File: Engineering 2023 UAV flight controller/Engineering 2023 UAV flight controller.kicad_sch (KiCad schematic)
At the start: 86 parts, among them J1 Micro_SD_Card, J2 ESC speed control, J3 USB_C_Receptacle_USB2.0, J4 Conn_Coaxial, J5 external power rail, J6 Board GPIO and the Lora DIO, J7 external ground rail, M1 Aileron Left, M2 Aileron Right, M3 Elevator Left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

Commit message: pcb revision one completed, the png's are for the reddit gods to review.
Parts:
- removed J6: Board GPIO and the Lora DIO, Connector_PinHeader_2.54mm:PinHeader_1x13_P2.54mm_Vertical, symbol Connector_Generic:Conn_01x13
- added H1, H2, H3: MountingHole, MountingHole:MountingHole_3.2mm_M3, symbol Mechanical:MountingHole
- added J10: DIO, Connector_PinHeader_2.54mm:PinHeader_1x03_P2.54mm_Vertical, symbol Connector_Generic:Conn_01x03
- added J6: GPIO, Connector_PinHeader_2.54mm:PinHeader_1x10_P2.54mm_Vertical, symbol Connector_Generic:Conn_01x10
- added J8: Serial wire debug, Connector_PinHeader_2.54mm:PinHeader_1x02_P2.54mm_Vertical, symbol Connector_Generic:Conn_01x02
- added J9: reset short?, Connector_PinHeader_2.54mm:PinHeader_1x02_P2.54mm_Vertical, symbol Connector_Generic:Conn_01x02
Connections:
- net DIO1: now also J10.1 (Pin_1)
- net DIO2: now also J10.2 (Pin_2)
- net DIO3: now also J10.3 (Pin_3)
- net External_pin_1: now also J6.1 (Pin_1)
- net External_pin_10: now also J6.10 (Pin_10)
- net External_pin_2: now also J6.2 (Pin_2)
- net External_pin_3: now also J6.3 (Pin_3)
- net External_pin_4: now also J6.4 (Pin_4)
- net External_pin_5: now also J6.5 (Pin_5)
- net External_pin_6: now also J6.6 (Pin_6)
- net External_pin_7: now also J6.7 (Pin_7)
- net External_pin_8: now also J6.8 (Pin_8)
- net External_pin_9: now also J6.9 (Pin_9)
- net GND: now also J9.2 (Pin_2)
- net RUN: now also J9.1 (Pin_1)
- net SWCLK: now also J8.1 (Pin_1)
- net SWD: now also J8.2 (Pin_2)
- net IMU_decouple_cap renamed IMU_CPOUT
- net IMU_CPOUT: no longer C25.2, U6.10 (REGOUT)
- new net IMU_REGOUT: C25.2, U6.10 (REGOUT)
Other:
- note removed: "0.1u for pin 10 2n2 for pin 20"

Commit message: got some work to do
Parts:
- removed C2, C6: 0.1uf, Capacitor_SMD:C_0603_1608Metric, symbol Device:C
- removed C5: 1uf, Capacitor_SMD:C_0603_1608Metric, symbol Device:C
- removed H1, H2, H3: MountingHole, MountingHole:MountingHole_3.2mm_M3, symbol Mechanical:MountingHole
- removed R1: R, Resistor_SMD:R_0603_1608Metric, symbol Device:R
- removed R2: R_Trim, Potentiometer_SMD:Potentiometer_Bourns_3314R-GM5_Vertical, symbol Device:R_Trim
- removed U3: LM350_TO220, Package_TO_SOT_THT:TO-220-3_Vertical, symbol Regulator_Linear:LM350_TO220
- added C?: 47u, symbol Device:C_Polarized_Small
- added J?: RFShield_OnePiece, symbol Device:RFShield_OnePiece
- C35: value 47p -> 10n
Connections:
- net GND: now also C?.2, J?.1 (Shield)
- net Servo 6V rail: now also C?.1; no longer D3.2 (A)
- net led_red: no longer names the net of D3.1 (K), R11.1
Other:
- note added: "switching regulator instead of linier reg"
- note removed: "R2/R1 = 4.8"

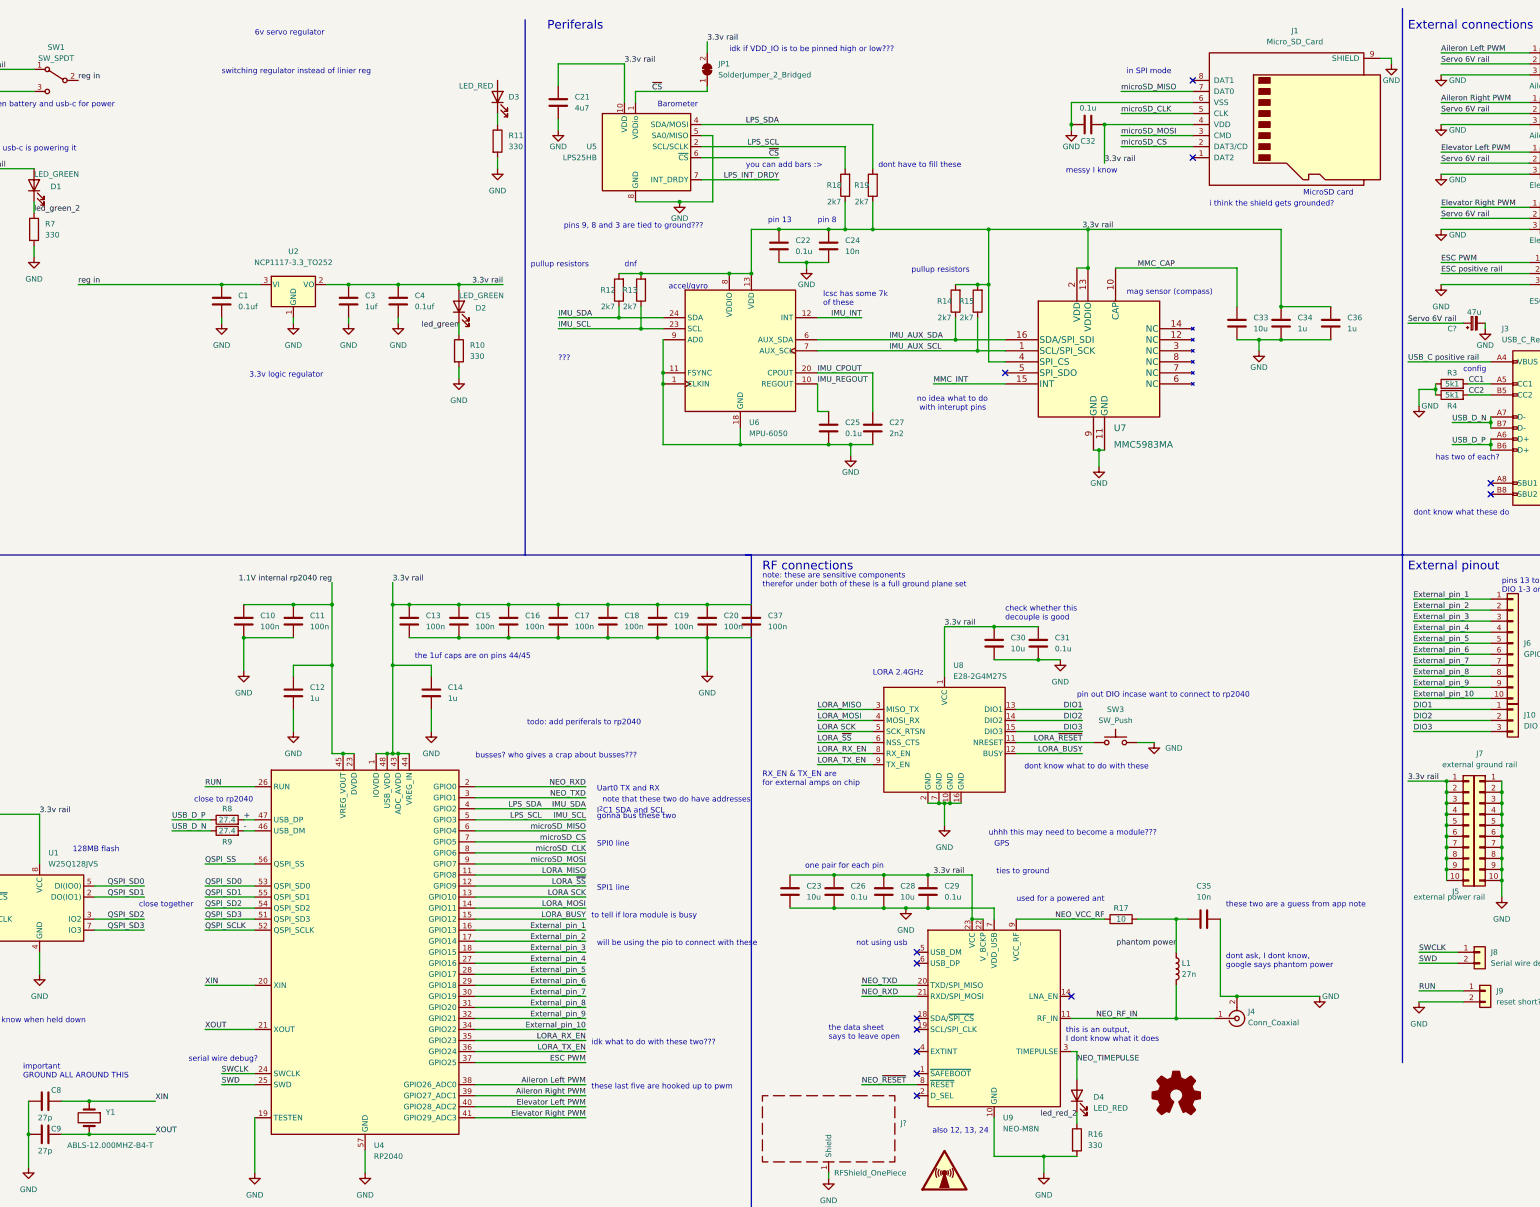
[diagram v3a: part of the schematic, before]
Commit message: added boost regulator
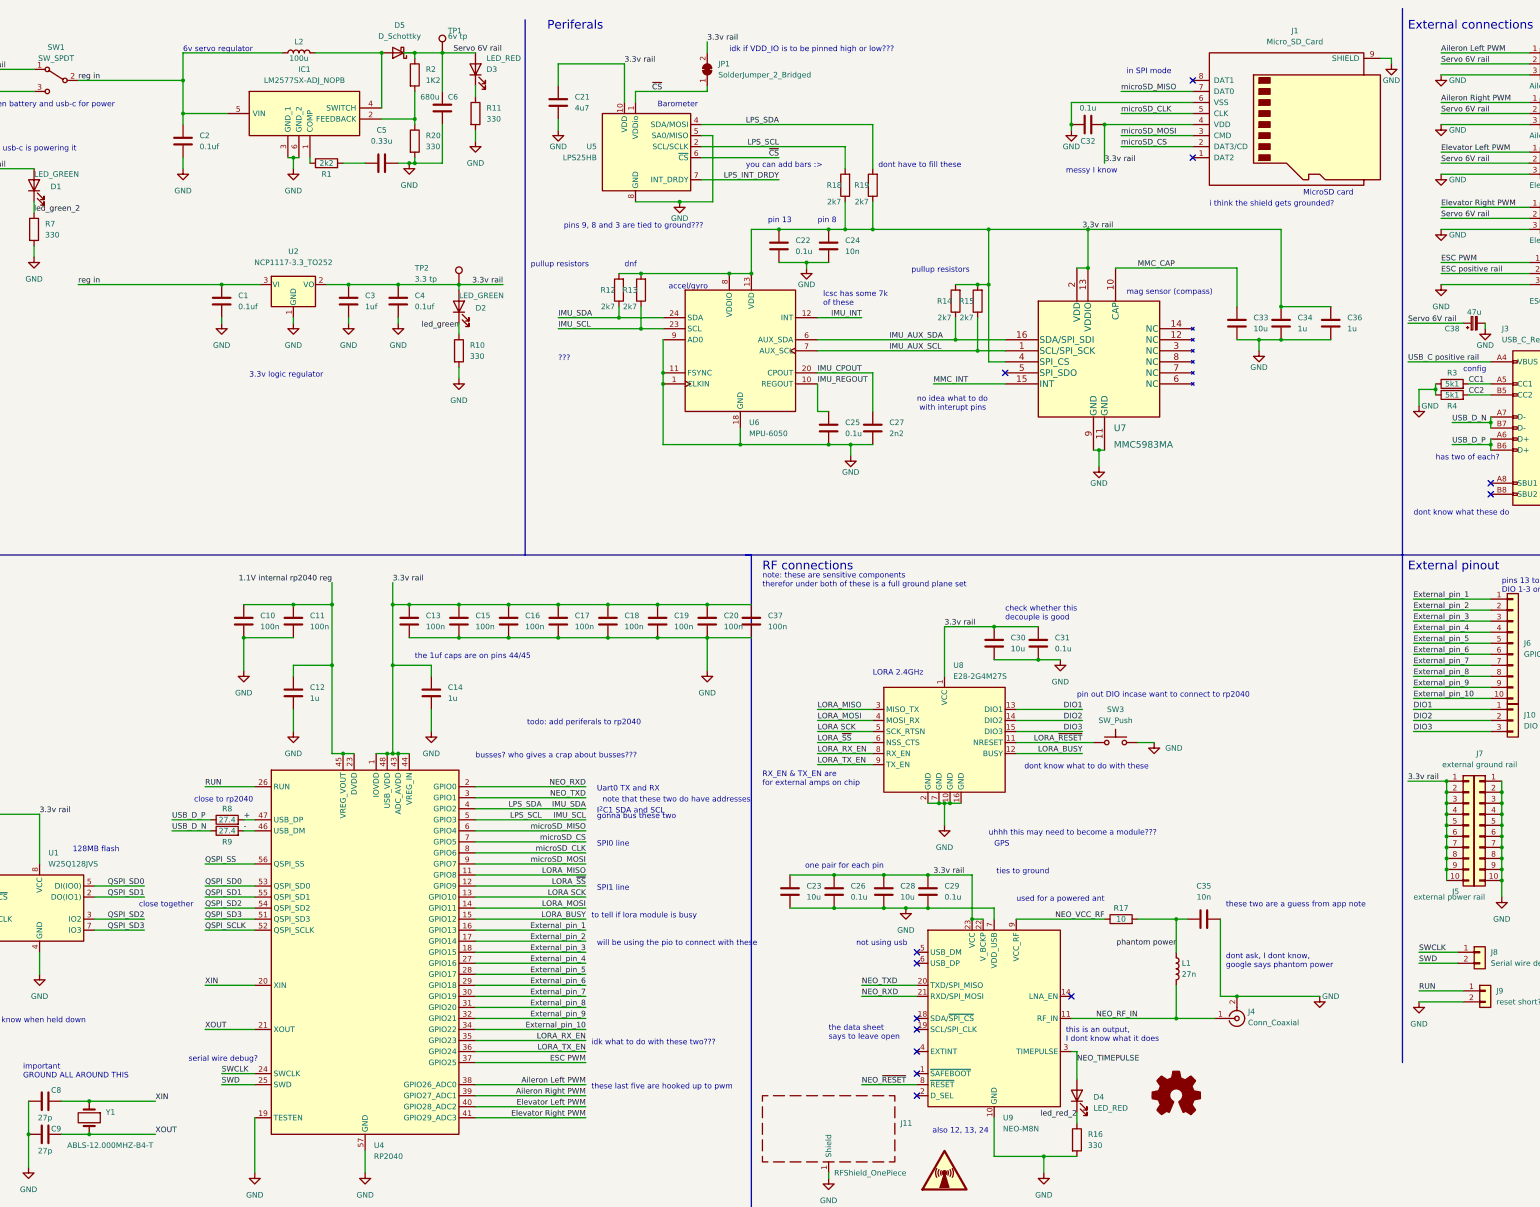
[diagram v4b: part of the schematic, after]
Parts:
- added C2: 0.1uf, Capacitor_SMD:C_0603_1608Metric, symbol Device:C
- added C5: 0.33u, Capacitor_SMD:C_0603_1608Metric, symbol Device:C
- added C6: 680u, Capacitor_SMD:C_0603_1608Metric, symbol Device:C
- added D5: D_Schottky, Diode_SMD:D_SMA, symbol Device:D_Schottky
- added IC1: LM2577SX-ADJ_NOPB, KTT0005B, symbol LM2577SX-ADJ_NOPB:LM2577SX-ADJ_NOPB
- added L2: 100u, symbol Device:L
- added R1: 2k2, Resistor_SMD:R_0603_1608Metric, symbol Device:R
- added R2: 1K2, Resistor_SMD:R_0603_1608Metric, symbol Device:R
- added R20: 330, Resistor_SMD:R_0603_1608Metric, symbol Device:R
- added TP1: 6v tp, TestPoint:TestPoint_Pad_D2.5mm, symbol Connector:TestPoint
- added TP2: 3.3 tp, TestPoint:TestPoint_Pad_D2.5mm, symbol Connector:TestPoint
- gave numbers to parts that had none: 2
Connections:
- net 3.3v rail: now also TP2.1
- net GND: now also C2.2, C5.2, C6.1, IC1.3 (GND_1), IC1.6 (GND_2), R20.2
- net Servo 6V rail: now also D3.2 (A), C6.2, D5.1 (K), R2.1, TP1.1
- net reg in: now also C2.1, IC1.5 (VIN), L2.1
- new net: IC1.2 (FEEDBACK), R2.2, R20.1
- new net: IC1.1 (COMP), R1.1
- new net: D5.2 (A), IC1.4 (SWITCH), L2.2
- new net: C5.1, R1.2
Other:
- note removed: "switching regulator instead of linier reg"
- moved on the sheet: D3, R11

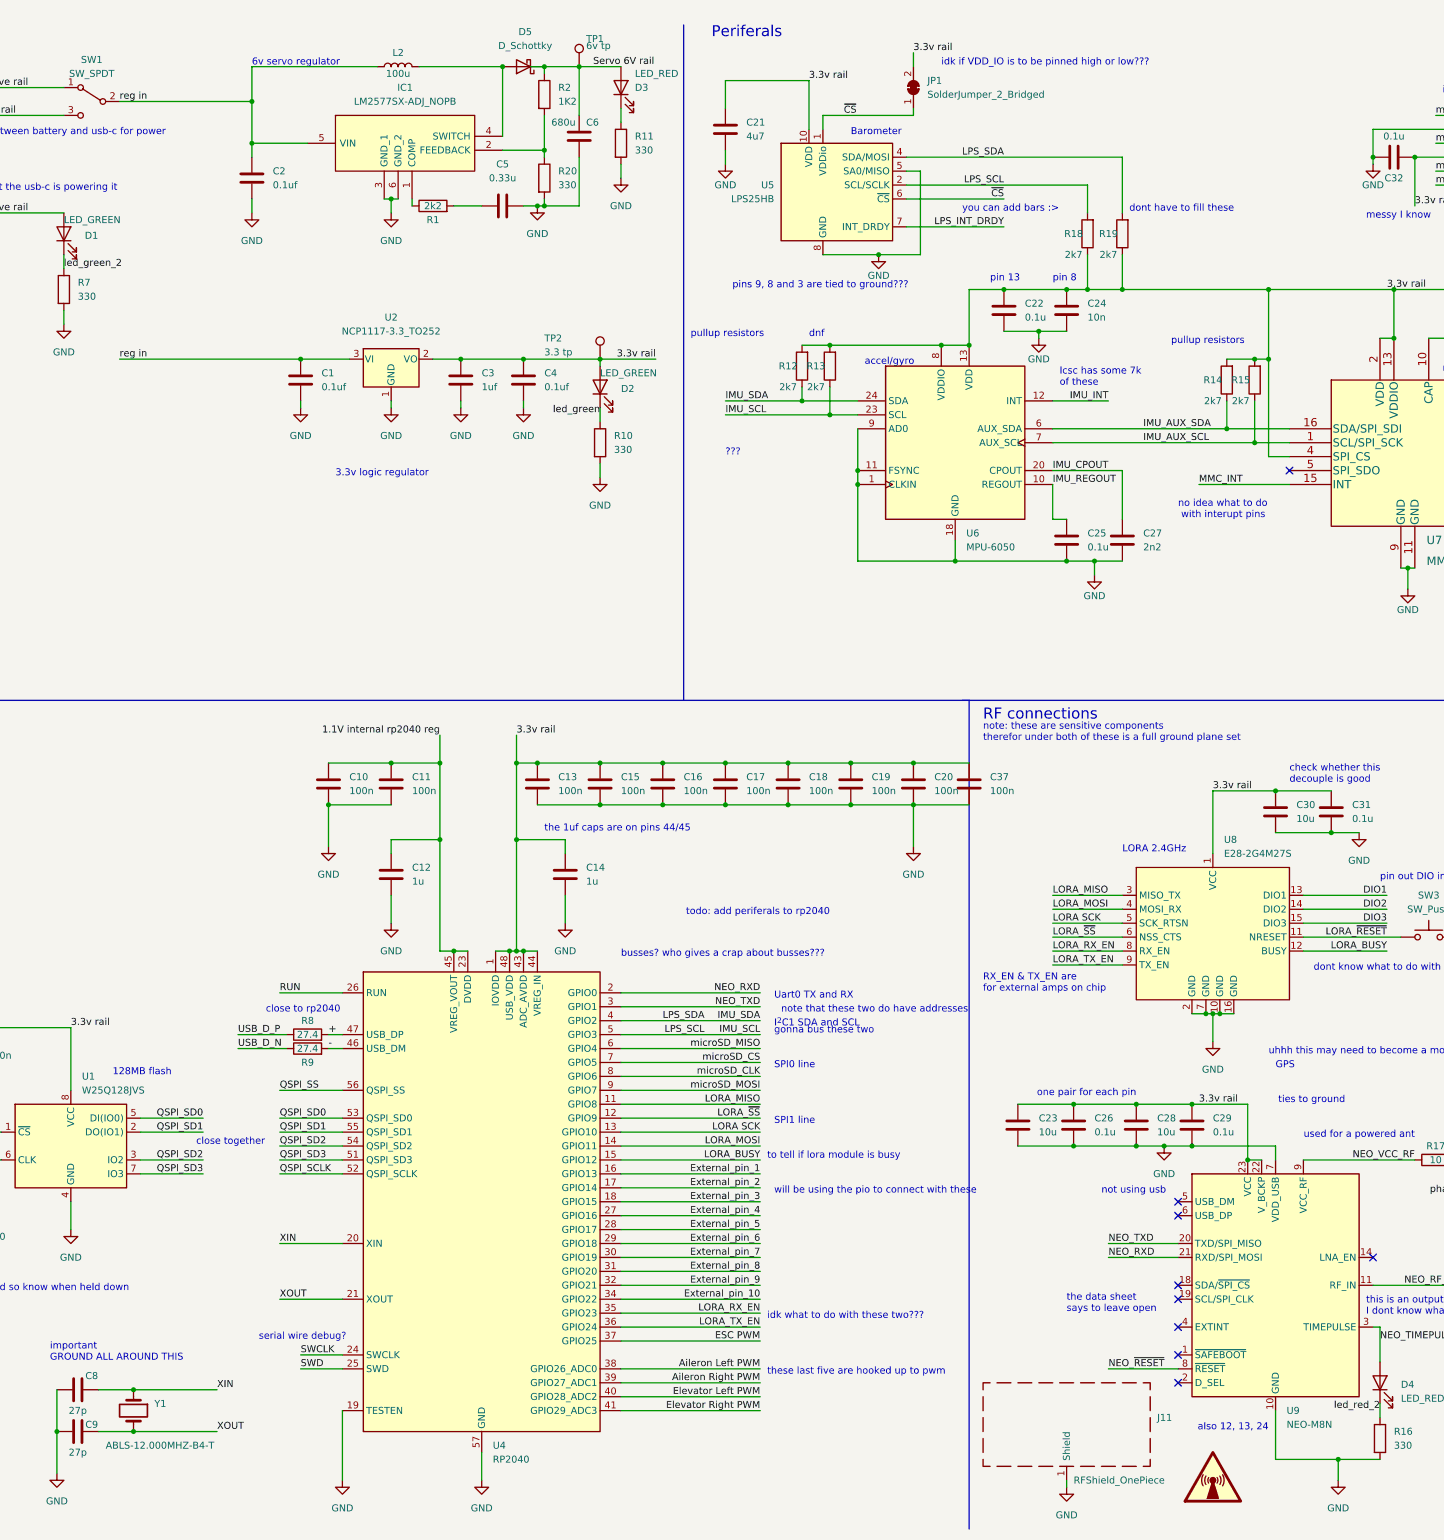
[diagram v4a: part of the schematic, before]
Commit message: started layout for the power part of board, addded some beads to NEO RX/TX
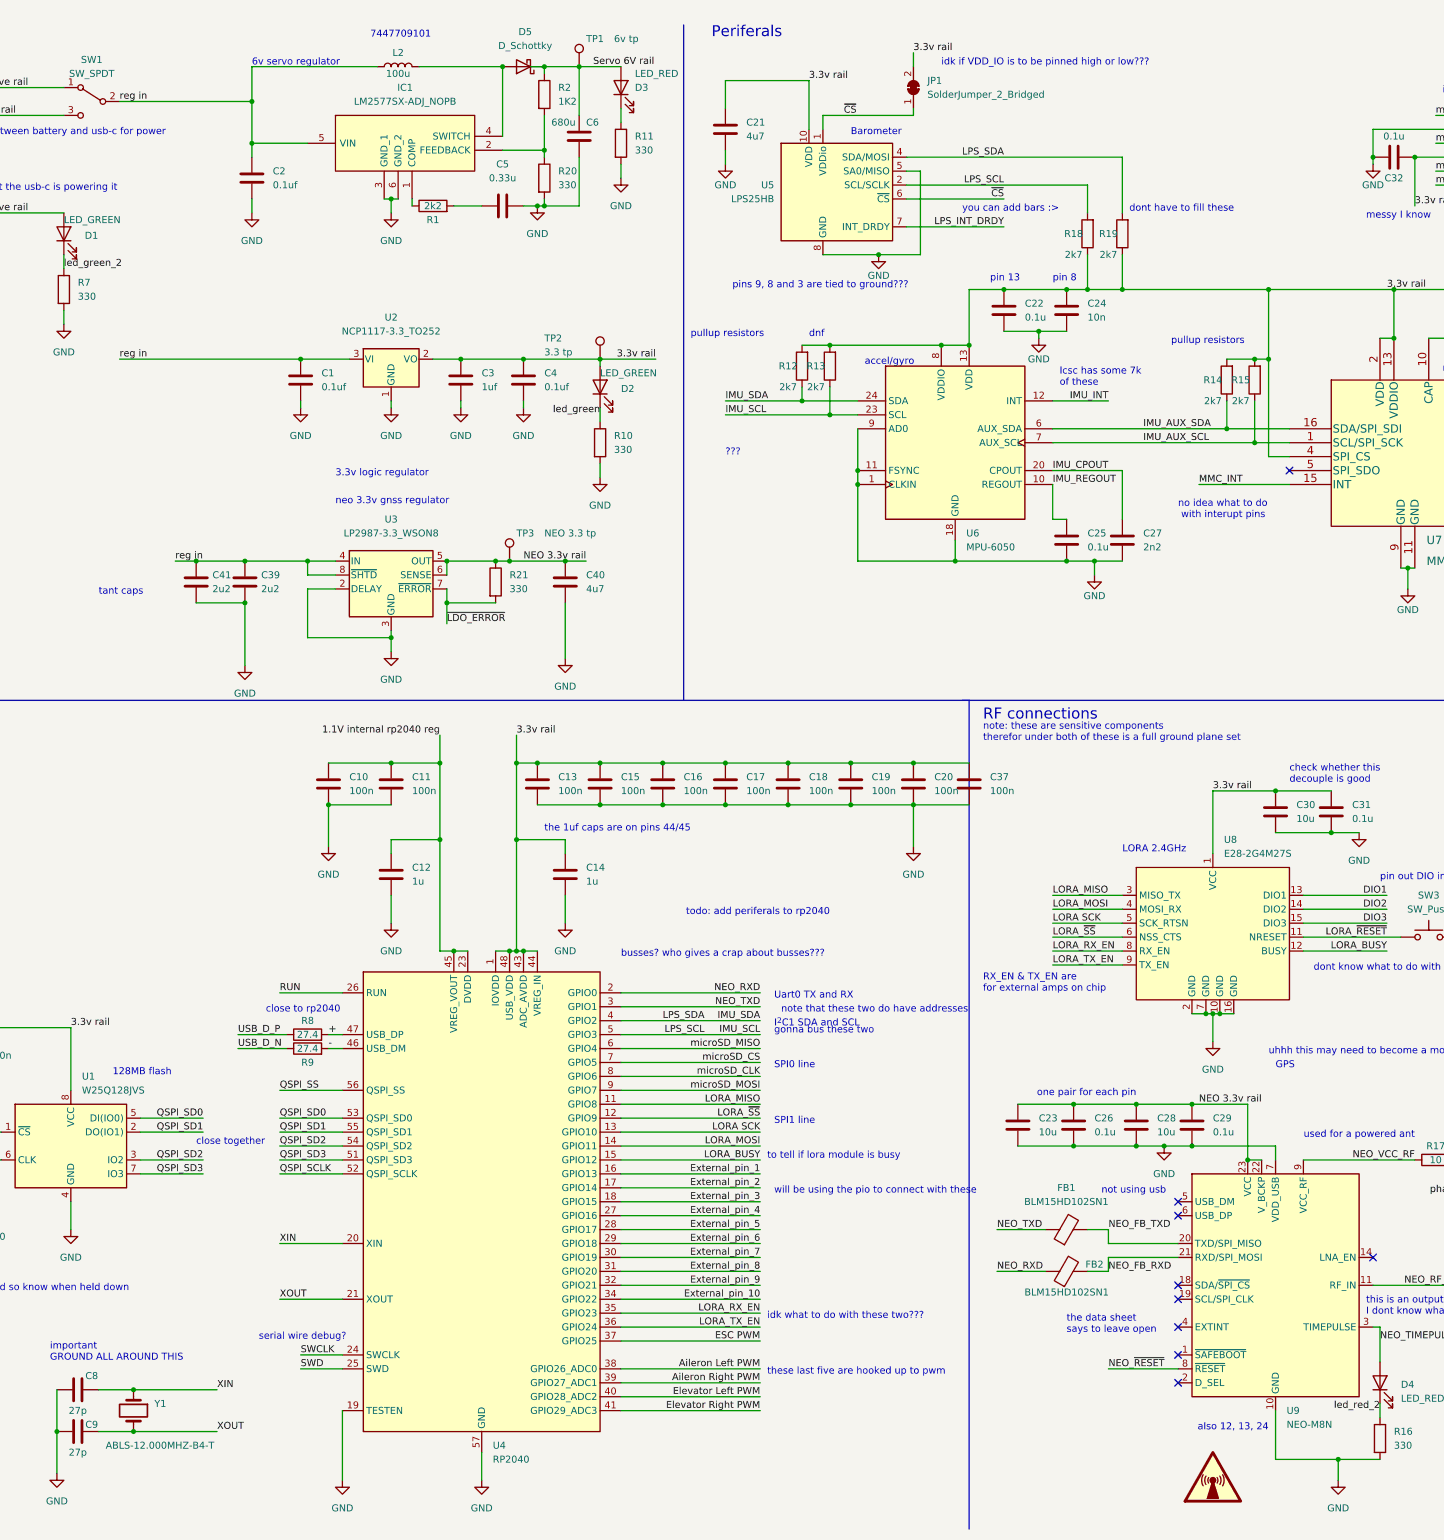
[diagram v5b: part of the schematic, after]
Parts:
- removed J11: RFShield_OnePiece, symbol Device:RFShield_OnePiece
- added C39, C41: 2u2, Capacitor_SMD:C_0603_1608Metric, symbol Device:C
- added C40: 4u7, Capacitor_SMD:C_0603_1608Metric, symbol Device:C
- added FB1, FB2: BLM15HD102SN1, Inductor_SMD:L_0402_1005Metric_Pad0.77x0.64mm_HandSolder, symbol Device:FerriteBead
- added R21: 330, Resistor_SMD:R_0603_1608Metric, symbol Device:R
- added TP3: NEO 3.3 tp, TestPoint:TestPoint_Pad_D2.5mm, symbol Connector:TestPoint
- added U3: LP2987-3.3_WSON8, Package_SON:WSON-8-1EP_4x4mm_P0.8mm_EP2.2x3mm, symbol Regulator_Linear:LP2987-3.3_WSON8
- C38: footprint (none) -> Capacitor_SMD:C_0603_1608Metric
- IC1: footprint KTT0005B -> Package_TO_SOT_THT:TO-220-5_Horizontal_TabDown
- L2: footprint (none) -> Inductor_SMD:L_Wuerth_WE-PD-Typ-LS
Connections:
- net 3.3v rail: no longer C23.1, C26.1, C28.1, C29.1, U9.22 (V_BCKP), U9.23 (VCC)
- net GND: now also C39.2, C40.2, C41.2, U3.2 (DELAY), U3.3 (GND), U3.9 (GND)
- net NEO_RXD: now also FB2.1; no longer U9.21 (RXD/SPI_MOSI)
- net NEO_TXD: now also FB1.1; no longer U9.20 (TXD/SPI_MISO)
- net reg in: now also C39.1, C41.1, U3.4 (IN), U3.8 (~{SHTD})
- new net NEO 3.3v rail: C23.1, C26.1, C28.1, C29.1, C40.1, R21.1, TP3.1, U3.5 (OUT), U3.6 (SENSE), U9.22 (V_BCKP), U9.23 (VCC)
- new net NEO_FB_RXD: FB2.2, U9.21 (RXD/SPI_MOSI)
- new net NEO_FB_TXD: FB1.2, U9.20 (TXD/SPI_MISO)
- new net ~{LDO_ERROR}: R21.2, U3.7 (~{ERROR})
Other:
- note added: "7447709101"
- note added: "neo 3.3v gnss regulator"
- note added: "tant caps"
- note removed: "ties to ground"
